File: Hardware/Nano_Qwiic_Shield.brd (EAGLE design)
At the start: 17.8 x 43.2 mm, 29 parts, among them J1 QWIIC_RIGHT_ANGLE, J2 QWIIC_RIGHT_ANGLE, J3 Vertical Qwiic Connector, J4 Vertical Qwiic Connector, U1 NANO_FOOTPRINT

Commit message: Initial commit/run of checklist
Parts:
- added U$14: (no value), buzzard_labels (18):NANO1
- added U$15: (no value), buzzard_labels (17):QWIIC_SHIELD1
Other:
- board text added: "A. England"
- board text added: "v10"
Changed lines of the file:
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@@
 <setting verticaltext="up"/>
 </settings>
-<grid distance="50" unitdist="mil" unit="inch" style="lines" multiple="1" display="yes" altdistance="5" altunitdist="mil" altunit="inch"/>
+<grid distance="0.05" unitdist="inch" unit="inch" style="lines" multiple="1" display="yes" altdistance="5" altunitdist="mil" altunit="inch"/>
 <layers>
 <layer number="1" name="Top" color="4" fill="1" visible="yes" active="yes"/>
@@
 <layer number="45" name="Holes" color="7" fill="1" visible="no" active="yes"/>
 <layer number="46" name="Milling" color="3" fill="1" visible="no" active="yes"/>
-<layer number="47" name="Measures" color="7" fill="1" visible="no" active="yes"/>
+<layer number="47" name="Measures" color="7" fill="1" visible="yes" active="yes"/>
 <layer number="48" name="Document" color="7" fill="1" visible="yes" active="yes"/>
 <layer number="49" name="Reference" color="7" fill="1" visible="yes" active="yes"/>
@@
 <wire x1="17.78" y1="43.18" x2="0" y2="43.18" width="0.2032" layer="20"/>
 <wire x1="0" y1="43.18" x2="0" y2="0" width="0.2032" layer="20"/>
+<text x="13.97" y="-7.62" size="1.778" layer="51" font="vector">A. England</text>
+<text x="10.795" y="0.254" size="1.778" layer="16" font="vector" ratio="15" rot="MR0">v10</text>
+<dimension x1="17.78" y1="43.18" x2="0" y2="43.18" x3="8.89" y3="44.45" textsize="1.27" textratio="15" layer="47" unit="inch"/>
+<dimension x1="17.78" y1="0" x2="17.78" y2="43.18" x3="20.32" y3="21.59" textsize="1.27" textratio="15" layer="47" unit="inch"/>
 </plain>
 <attributes>
@@
 <element name="FD3" library="SparkFun-Aesthetics" package="FIDUCIAL-0.2MM" value="FIDUCIAL0.2MM" x="16.51" y="41.91"/>
 <element name="FD4" library="SparkFun-Aesthetics" package="FIDUCIAL-0.2MM" value="FIDUCIAL0.2MM" x="16.51" y="41.91" rot="MR0"/>
+<element name="U$14" library="buzzard_labels (18)" package="NANO1" value="" x="11.557" y="10.16" rot="MR0"/>
+<element name="U$15" library="buzzard_labels (17)" package="QWIIC_SHIELD1" value="" x="13.97" y="8.636" rot="MR0"/>
 </elements>
 <signals>

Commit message: post review changes
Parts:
- FD1, FD2, FD3, FD4: value FIDUCIAL0.2MM -> FIDUCIAL1X2; device SparkFun-Aesthetics:FIDUCIAL-0.2MM -> SparkFun-Aesthetics:FIDUCIAL-1X2
- moved FD1 1.80 mm to (2.54, 2.54)
- moved FD2 1.80 mm to (2.54, 2.54)
- moved FD3 1.80 mm to (15.2, 40.6)
- moved FD4 1.80 mm to (15.2, 40.6)
- moved LOGO2 0.51 mm to (8.89, 16.5)
- renumbered U1 to J5
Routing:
- net SCL: track 43.7 -> 42.9 mm
- net SDA: track 50.2 -> 49.5 mm
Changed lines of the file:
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@@
 <layer number="43" name="vRestrict" color="2" fill="10" visible="yes" active="yes"/>
 <layer number="44" name="Drills" color="7" fill="1" visible="no" active="yes"/>
-<layer number="45" name="Holes" color="7" fill="1" visible="no" active="yes"/>
+<layer number="45" name="Holes" color="7" fill="1" visible="yes" active="yes"/>
 <layer number="46" name="Milling" color="3" fill="1" visible="no" active="yes"/>
 <layer number="47" name="Measures" color="7" fill="1" visible="yes" active="yes"/>
@@
 <dimension x1="17.78" y1="43.18" x2="0" y2="43.18" x3="8.89" y3="44.45" textsize="1.27" textratio="15" layer="47" unit="inch"/>
 <dimension x1="17.78" y1="0" x2="17.78" y2="43.18" x3="20.32" y3="21.59" textsize="1.27" textratio="15" layer="47" unit="inch"/>
+<hole x="1.27" y="41.91" drill="1.778"/>
+<hole x="16.51" y="41.91" drill="1.778"/>
+<hole x="16.51" y="1.27" drill="1.778"/>
+<hole x="1.27" y="1.27" drill="1.778"/>
 </plain>
 <attributes>
@@
 <attribute name="REV" value="" x="-12.7" y="-7.62" size="1.778" layer="27" display="off"/>
 </element>
-<element name="U1" library="SparkFun-Boards" package="NANO" value="NANO_FOOTPRINT" x="8.89" y="21.59"/>
+<element name="J5" library="SparkFun-Boards" package="NANO" value="NANO_FOOTPRINT" x="8.89" y="21.59"/>
 <element name="I2C" library="SparkFun-Jumpers" package="SMT-JUMPER_3_NO_NO-SILK" package3d_urn="urn:adsk.eagle:package:39284/1" value="JUMPER-SMT_3_NO_NO-SILK" x="8.89" y="21.59" rot="R180"/>
 <element name="R1" library="SparkFun-Resistors" package="0603" value="4.7k" x="11.43" y="21.59" rot="R270">
@@
 </element>
 <element name="LOGO1" library="SparkFun-Aesthetics" package="OSHW-LOGO-S" value="OSHW-LOGOS" x="8.89" y="2.54" rot="MR0"/>
-<element name="LOGO2" library="SparkFun-Aesthetics" package="SFE_LOGO_NAME_FLAME_.1" value="SFE_LOGO_NAME_FLAME.1_INCH" x="8.89" y="17.018"/>
+<element name="LOGO2" library="SparkFun-Aesthetics" package="SFE_LOGO_NAME_FLAME_.1" value="SFE_LOGO_NAME_FLAME.1_INCH" x="8.89" y="16.51"/>
 <element name="LOGO3" library="SparkFun-Aesthetics" package="SFE_LOGO_NAME_FLAME_.1" value="SFE_LOGO_NAME_FLAME.1_INCH" x="8.763" y="17.145" rot="MR0"/>
 <element name="U$1" library="buzzard_labels (17)" package="QWIIC_SHIELD1" value="" x="3.81" y="8.636"/>
@@
 <element name="U$12" library="buzzard_labels (23)" package="3V36" value="" x="11.811" y="6.35"/>
 <element name="U$13" library="buzzard_labels (23)" package="3V36" value="" x="16.51" y="6.35" rot="MR0"/>
-<element name="FD1" library="SparkFun-Aesthetics" package="FIDUCIAL-0.2MM" value="FIDUCIAL0.2MM" x="1.27" y="1.27"/>
-<element name="FD2" library="SparkFun-Aesthetics" package="FIDUCIAL-0.2MM" value="FIDUCIAL0.2MM" x="1.27" y="1.27" rot="MR0"/>
-<element name="FD3" library="SparkFun-Aesthetics" package="FIDUCIAL-0.2MM" value="FIDUCIAL0.2MM" x="16.51" y="41.91"/>
-<element name="FD4" library="SparkFun-Aesthetics" package="FIDUCIAL-0.2MM" value="FIDUCIAL0.2MM" x="16.51" y="41.91" rot="MR0"/>
+<element name="FD1" library="SparkFun-Aesthetics" package="FIDUCIAL-1X2" value="FIDUCIAL1X2" x="2.54" y="2.54"/>
+<element name="FD2" library="SparkFun-Aesthetics" package="FIDUCIAL-1X2" value="FIDUCIAL1X2" x="2.54" y="2.54" rot="MR0"/>
+<element name="FD3" library="SparkFun-Aesthetics" package="FIDUCIAL-1X2" value="FIDUCIAL1X2" x="15.24" y="40.64"/>
+<element name="FD4" library="SparkFun-Aesthetics" package="FIDUCIAL-1X2" value="FIDUCIAL1X2" x="15.24" y="40.64" rot="MR0"/>
 <element name="U$14" library="buzzard_labels (18)" package="NANO1" value="" x="11.557" y="10.16" rot="MR0"/>
 <element name="U$15" library="buzzard_labels (17)" package="QWIIC_SHIELD1" value="" x="13.97" y="8.636" rot="MR0"/>
@@
 <signals>
 <signal name="3.3V">
-<contactref element="U1" pad="17"/>
+<contactref element="J5" pad="17"/>
 <contactref element="I2C" pad="2"/>
 <contactref element="J1" pad="2"/>
@@
 </signal>
 <signal name="GND">
-<contactref element="U1" pad="4"/>
-<contactref element="U1" pad="29"/>
+<contactref element="J5" pad="4"/>
+<contactref element="J5" pad="29"/>
 <contactref element="J4" pad="1"/>
 <contactref element="J3" pad="1"/>
@@
 <via x="6.35" y="10.16" extent="1-16" drill="0.381"/>
 <via x="6.35" y="6.35" extent="1-16" drill="0.381"/>
+<via x="7.62" y="24.13" extent="1-16" drill="0.381"/>
+<via x="7.62" y="19.05" extent="1-16" drill="0.381"/>
+<via x="10.16" y="19.05" extent="1-16" drill="0.381"/>
+<via x="10.16" y="24.13" extent="1-16" drill="0.381"/>
 </signal>
 <signal name="SCL">
-<contactref element="U1" pad="24"/>
+<contactref element="J5" pad="24"/>
 <contactref element="R1" pad="1"/>
 <contactref element="J1" pad="4"/>
@@
 <wire x1="7.39" y1="38.1" x2="7.39" y2="30.997" width="0.2032" layer="1"/>
 <wire x1="7.39" y1="30.997" x2="7.368" y2="30.975" width="0.2032" layer="1"/>
-<wire x1="10.16" y1="25.4" x2="11.43" y2="24.13" width="0.2032" layer="1"/>
-<wire x1="10.16" y1="25.4" x2="10.16" y2="29.21" width="0.2032" layer="1"/>
+<wire x1="10.16" y1="26.67" x2="12.7" y2="24.13" width="0.2032" layer="1"/>
+<wire x1="10.16" y1="26.67" x2="10.16" y2="29.21" width="0.2032" layer="1"/>
 <via x="10.16" y="29.21" extent="1-16" drill="0.381"/>
 <wire x1="10.16" y1="29.21" x2="7.366" y2="29.21" width="0.2032" layer="16"/>
@@
 <wire x1="7.366" y1="29.21" x2="7.368" y2="29.212" width="0.2032" layer="1"/>
 <wire x1="7.368" y1="29.212" x2="7.368" y2="30.975" width="0.2032" layer="1"/>
-<wire x1="11.43" y1="24.13" x2="12.7" y2="24.13" width="0.2032" layer="1"/>
 <wire x1="12.7" y1="24.13" x2="12.954" y2="24.13" width="0.2032" layer="1"/>
 <wire x1="12.954" y1="24.13" x2="16.51" y2="24.13" width="0.2032" layer="1"/>
@@
 </signal>
 <signal name="SDA">
-<contactref element="U1" pad="23"/>
+<contactref element="J5" pad="23"/>
 <contactref element="R2" pad="1"/>
 <contactref element="J1" pad="3"/>
@@
 <via x="7.493" y="14.605" extent="1-16" drill="0.381"/>
 <wire x1="8.89" y1="14.605" x2="7.493" y2="14.605" width="0.2032" layer="16"/>
-<wire x1="7.493" y1="14.605" x2="7.493" y2="17.907" width="0.2032" layer="1"/>
-<wire x1="7.493" y1="17.907" x2="6.35" y2="19.05" width="0.2032" layer="1"/>
-<wire x1="6.35" y1="19.05" x2="5.715" y2="19.05" width="0.2032" layer="1"/>
-<wire x1="4.865" y1="19.9" x2="5.715" y2="19.05" width="0.2032" layer="1"/>
+<wire x1="7.493" y1="14.605" x2="7.493" y2="17.272" width="0.2032" layer="1"/>
+<wire x1="7.493" y1="17.272" x2="4.865" y2="19.9" width="0.2032" layer="1"/>
 <wire x1="8.39" y1="38.1" x2="8.39" y2="30.997" width="0.2032" layer="1"/>
 <wire x1="8.39" y1="30.997" x2="8.368" y2="30.975" width="0.2032" layer="1"/>
-<wire x1="8.368" y1="30.975" x2="8.368" y2="26.148" width="0.2032" layer="1"/>
-<wire x1="6.35" y1="24.13" x2="5.715" y2="24.13" width="0.2032" layer="1"/>
-<wire x1="5.715" y1="24.13" x2="4.865" y2="23.28" width="0.2032" layer="1"/>
-<wire x1="8.368" y1="26.148" x2="6.35" y2="24.13" width="0.2032" layer="1"/>
+<wire x1="8.368" y1="30.975" x2="8.368" y2="26.783" width="0.2032" layer="1"/>
+<wire x1="8.368" y1="26.783" x2="4.865" y2="23.28" width="0.2032" layer="1"/>
 <wire x1="16.51" y1="21.59" x2="9.525" y2="14.605" width="0.2032" layer="16"/>
 <wire x1="9.525" y1="14.605" x2="8.89" y2="14.605" width="0.2032" layer="16"/>

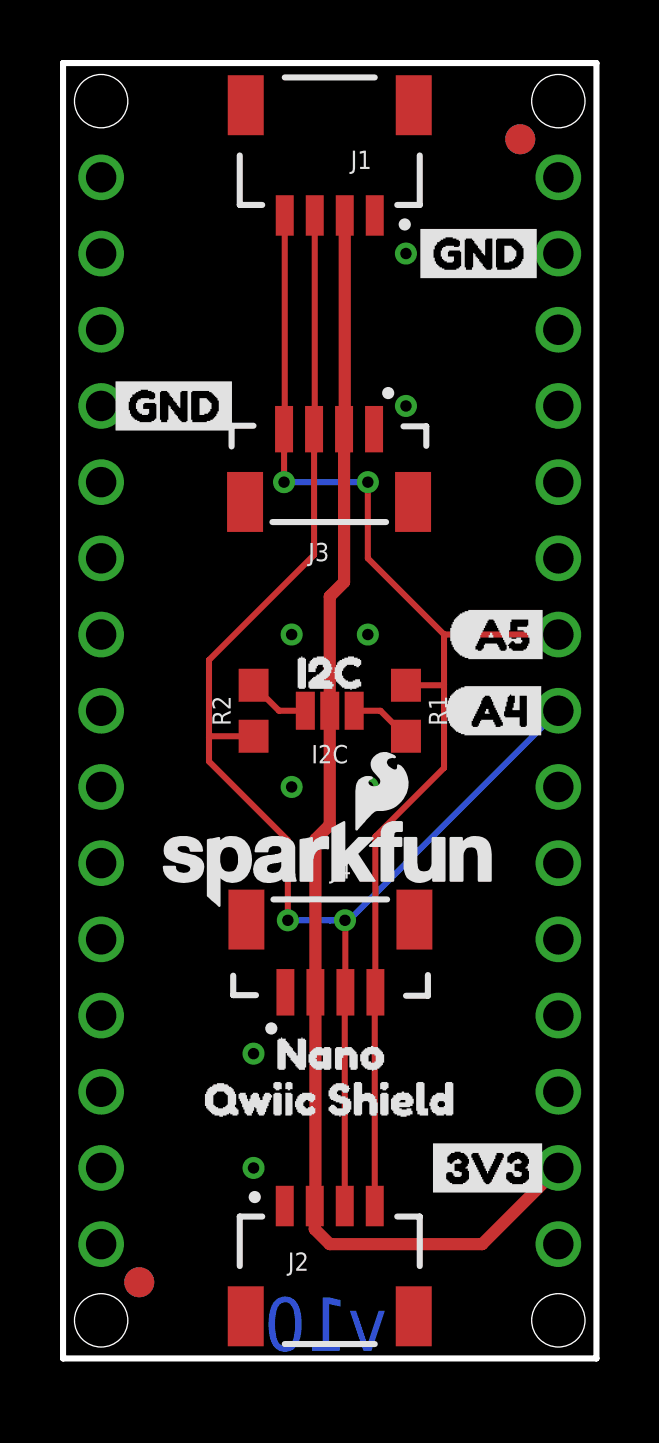
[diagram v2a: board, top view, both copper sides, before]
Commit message: adding conversion circuitry
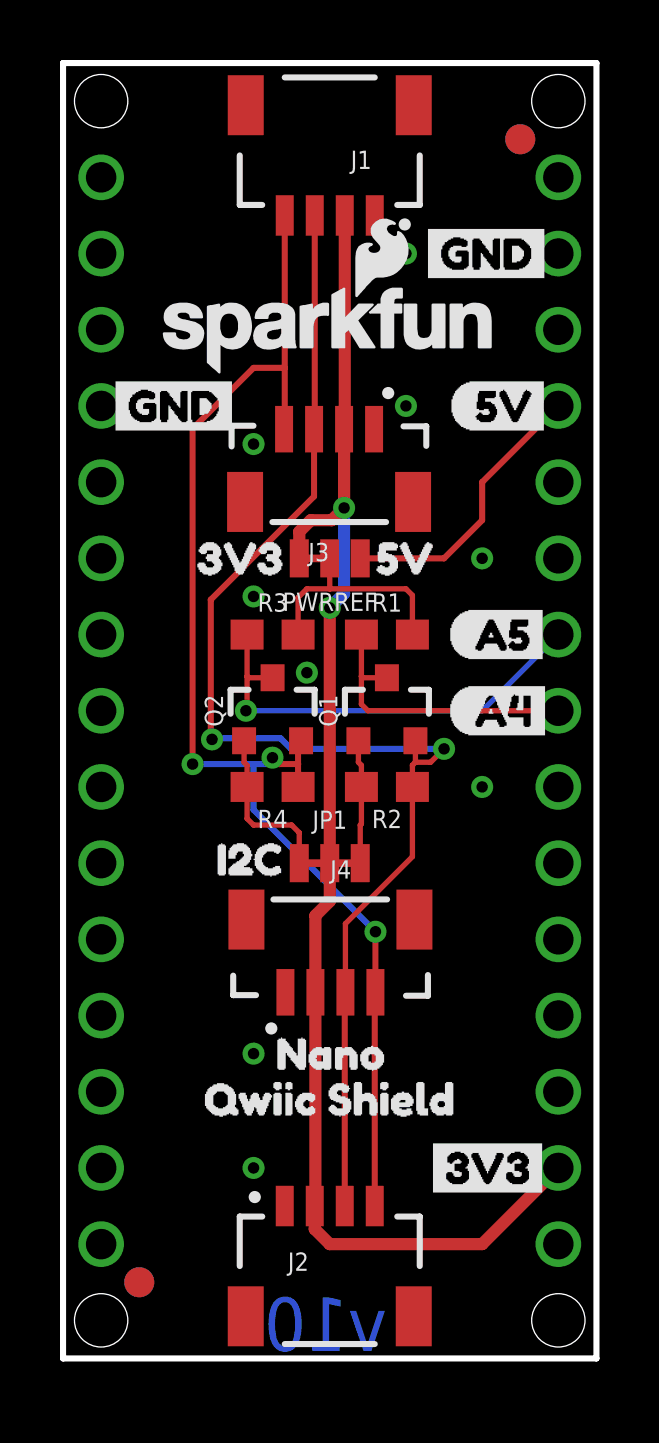
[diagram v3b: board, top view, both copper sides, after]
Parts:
- removed I2C: JUMPER-SMT_3_NO_NO-SILK, SparkFun-Jumpers:SMT-JUMPER_3_NO_NO-SILK
- added JP1: JUMPER-SMT_3_2-NC_TRACE_NO-SILK, SparkFun-Jumpers:SMT-JUMPER_3_2-NC_TRACE_NO-SILK
- added PWRREF: JUMPER-SMT_3_1-NC_TRACE_NO-SILK, SparkFun-Jumpers:SMT-JUMPER_3_1-NC_TRACE_NO-SILK
- added Q1, Q2: 220mA/50V/3.5Ω, SparkFun-DiscreteSemi:SOT23-3
- added R3, R4: 4.7k, SparkFun-Resistors:0603
- added U$16: (no value), buzzard_labels (27):3V31
- added U$17: (no value), buzzard_labels (27):5V0
- added U$18: (no value), buzzard_labels (28):5V0
- added U$19: (no value), buzzard_labels (28):5V1
- moved LOGO2 17.8 mm to (8.89, 34.3)
- moved U$11 6.77 mm to (4.19, 16.6)
- moved R2 5.12 mm to (10.8, 19.1), turned to 180 degrees
- moved R1 2.62 mm to (10.8, 24.1), turned to 0 degrees
- moved U$7 0.25 mm to (16.5, 36.8)
- moved U$6 0.25 mm to (11.7, 36.8)
- moved U$9 0.13 mm to (12.8, 21.6)
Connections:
- removed net N$1: I2C.3, R2.2
- removed net N$2: I2C.1, R1.2
- new net 5V: J5.27, PWRREF.1
- new net HV_SCL: J5.24, Q2.3, R3.1
- new net HV_SDA: J5.23, Q1.3, R1.1
- new net IOREF: PWRREF.2, R1.2, R3.2
- new net SCLJUMP: JP1.1, Q2.1, R4.2
- new net SDAJUMP: JP1.3, Q1.1, R2.2
- net 3.3V: now also JP1.2, PWRREF.3; no longer I2C.2
- net SCL: now also Q2.2, R4.1; no longer J5.24, R1.1
- net SDA: now also Q1.2; no longer J5.23
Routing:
- net HV_SCL: track 0.00 -> 14.9 mm, vias 0 -> 1
- net HV_SDA: track 0.00 -> 9.85 mm
- net 5V: track 0.00 -> 9.45 mm
- net IOREF: track 0.00 -> 7.58 mm
- net SCLJUMP: track 0.00 -> 5.59 mm
- net SDA: track 49.5 -> 44.4 mm
- net SDAJUMP: track 0.00 -> 4.14 mm
- net 3.3V: track 43.6 -> 46.3 mm, vias 0 -> 2
- net N$2: track 2.08 -> 0.00 mm
- net N$1: track 2.08 -> 0.00 mm
- net SCL: track 42.9 -> 43.9 mm, vias 2 -> 3
